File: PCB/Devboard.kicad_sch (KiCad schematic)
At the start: 33 parts, among them J1 USB_C_Receptacle_USB2.0_14P, J2 Conn_01x20, J3 Conn_01x20, J4 Conn_01x03, SW1 SW_Push, U1 RP2040, U2 NCP1117-3.3_SOT223, U3 W25Q16JVZPIQ TR, Y1 12 MHz

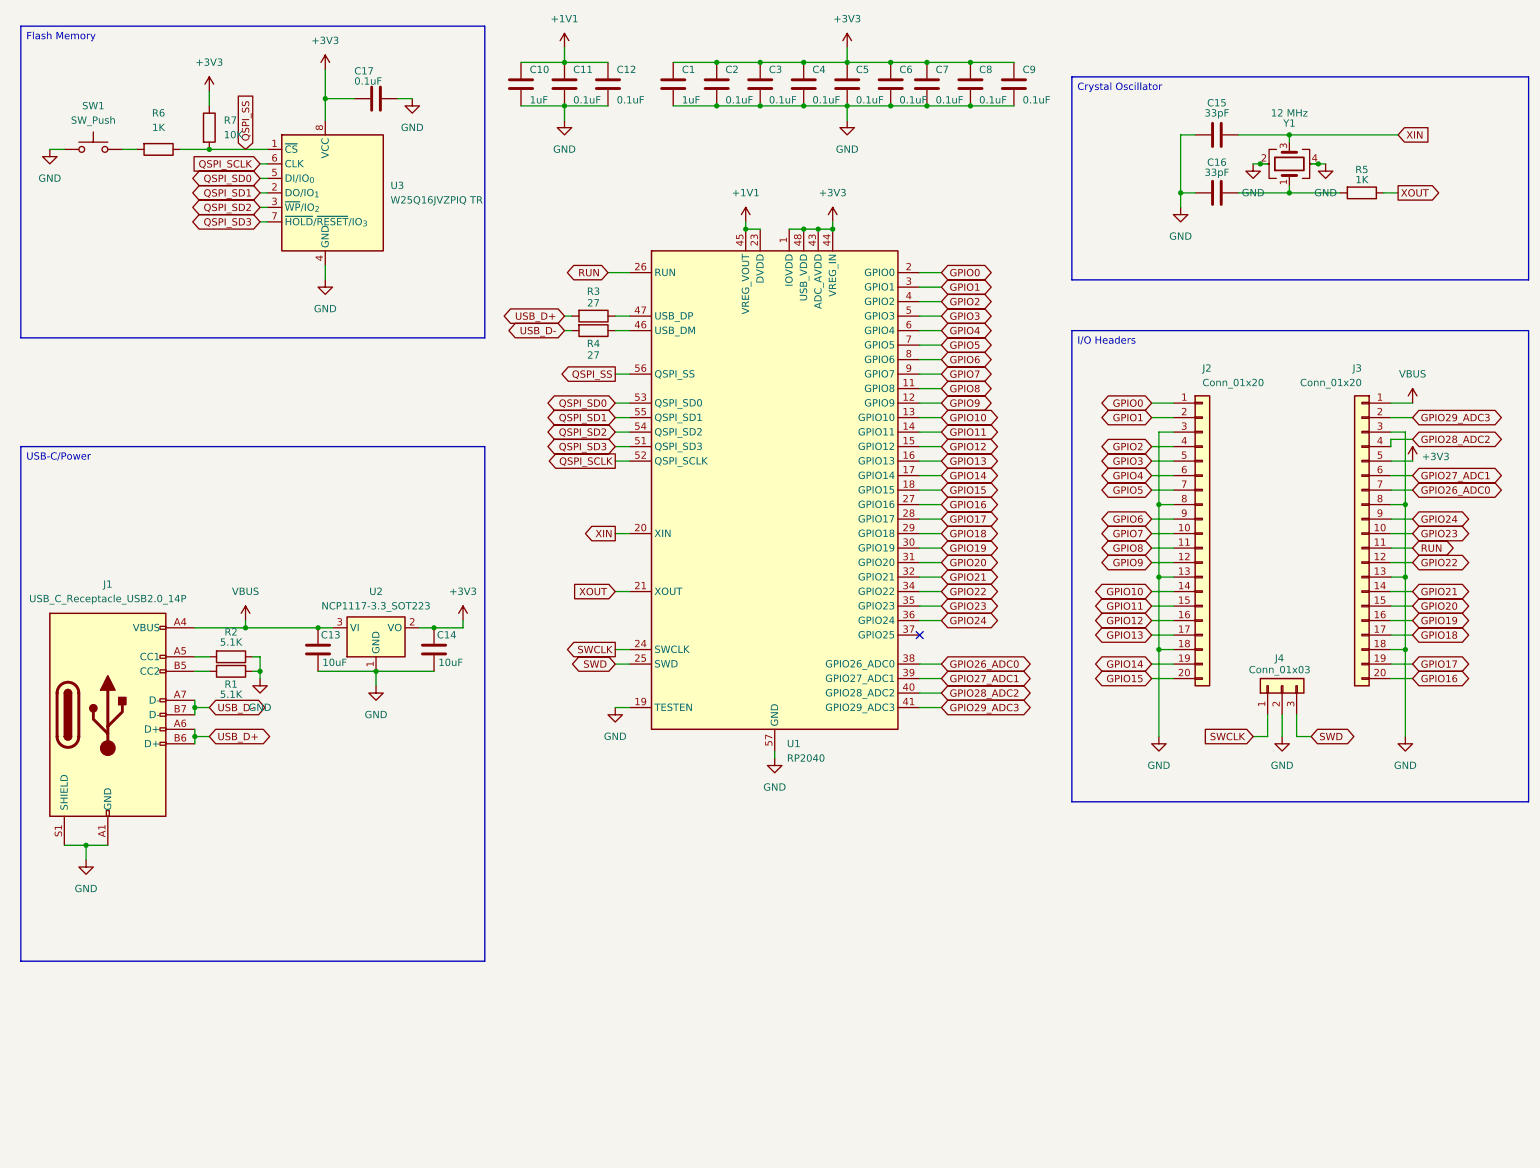
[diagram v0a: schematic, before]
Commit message: added temperature sensor
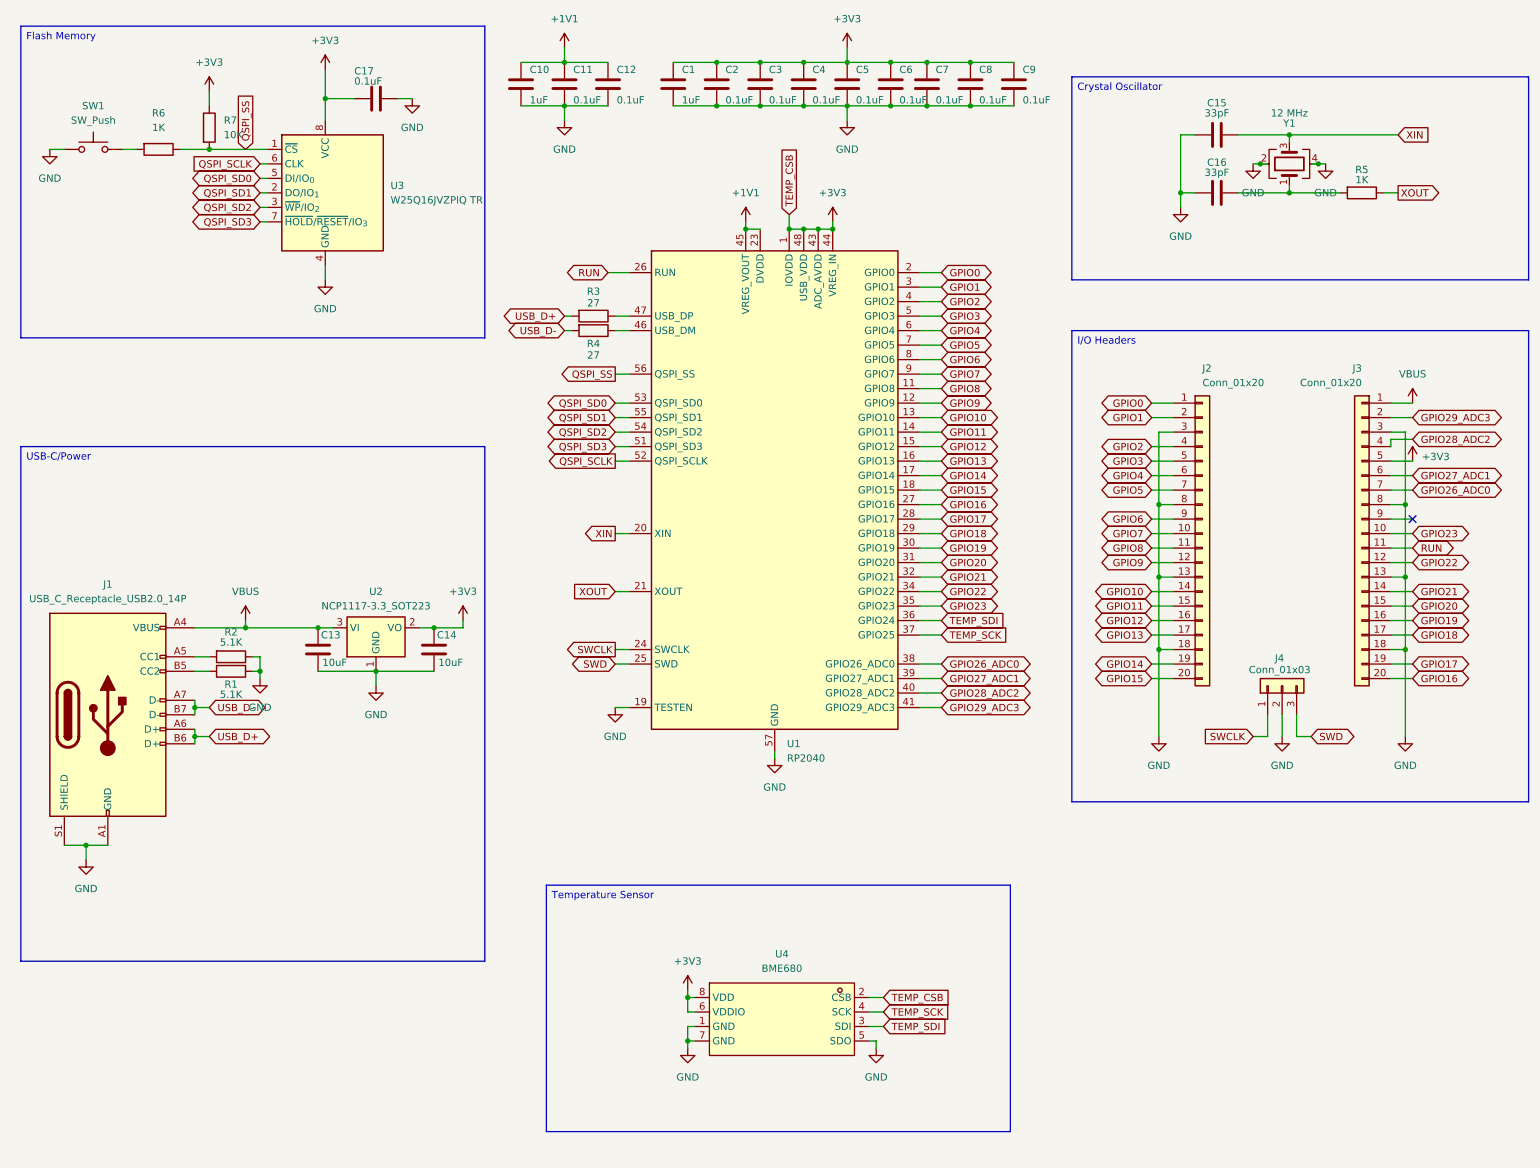
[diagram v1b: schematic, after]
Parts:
- added U4: BME680, lcsc2:LGA-8_L3.0-W3.0-P0.80-TR, symbol lcsc2:BME680
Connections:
- net +3V3: now also U4.2 (CSB), U4.6 (VDDIO), U4.8 (VDD)
- net GND: now also U4.1 (GND), U4.5 (SDO), U4.7 (GND)
- net TEMP_SCK: now reaches U1.37 (GPIO25)
- net TEMP_SCK: now also U4.4 (SCK)
- net GPIO24: no longer names the net of J3.9 (Pin_9)
- net GPIO24: no longer U1.36 (GPIO24)
- new net TEMP_SDI: U1.36 (GPIO24), U4.3 (SDI)

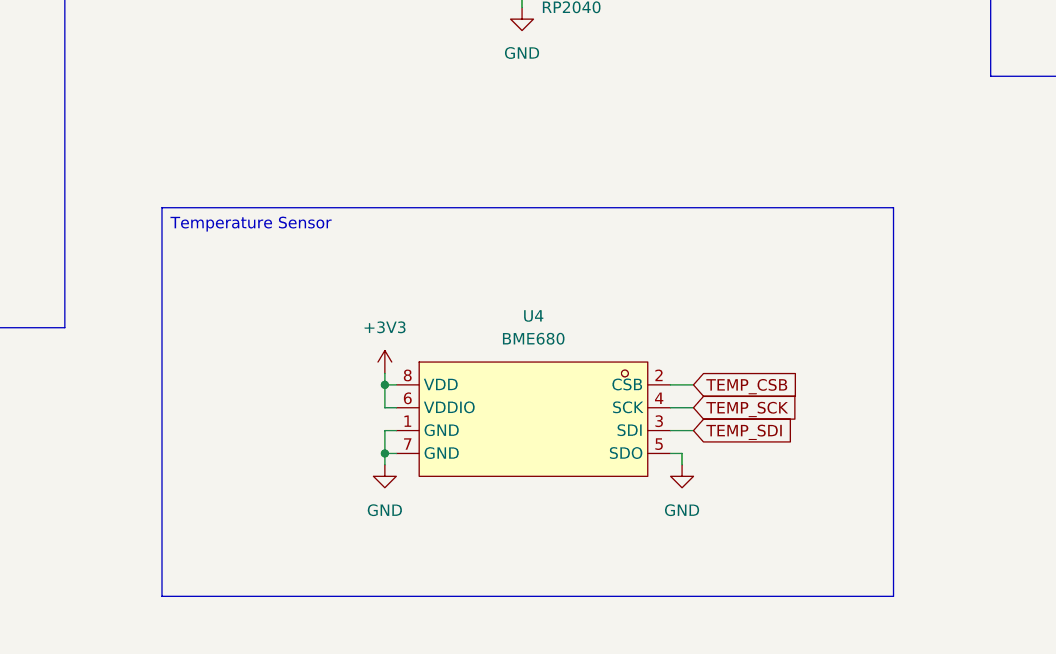
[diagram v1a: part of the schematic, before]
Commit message: changed temperature sensor
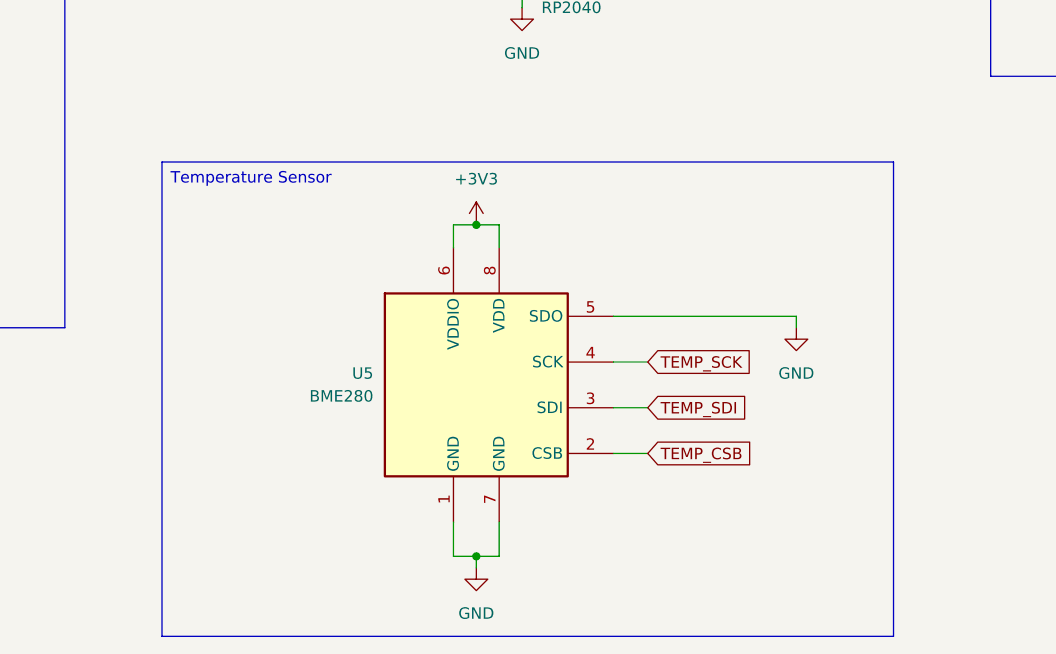
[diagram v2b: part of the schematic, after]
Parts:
- removed U4: BME680, lcsc2:LGA-8_L3.0-W3.0-P0.80-TR, symbol lcsc2:BME680
- added U5: BME280, Package_LGA:Bosch_LGA-8_2.5x2.5mm_P0.65mm_ClockwisePinNumbering, symbol Sensor:BME280
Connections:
- net +3V3: now also U5.2 (CSB), U5.6 (VDDIO), U5.8 (VDD)
- net GND: now also U5.1 (GND), U5.5 (SDO), U5.7 (GND)
- net TEMP_SCK: now also U5.4 (SCK)
- net TEMP_SDI: now also U5.3 (SDI)
